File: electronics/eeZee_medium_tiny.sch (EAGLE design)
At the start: 11 parts, among them IC1 TINY24/44/84, J2 avrisp, Q1 16MHz

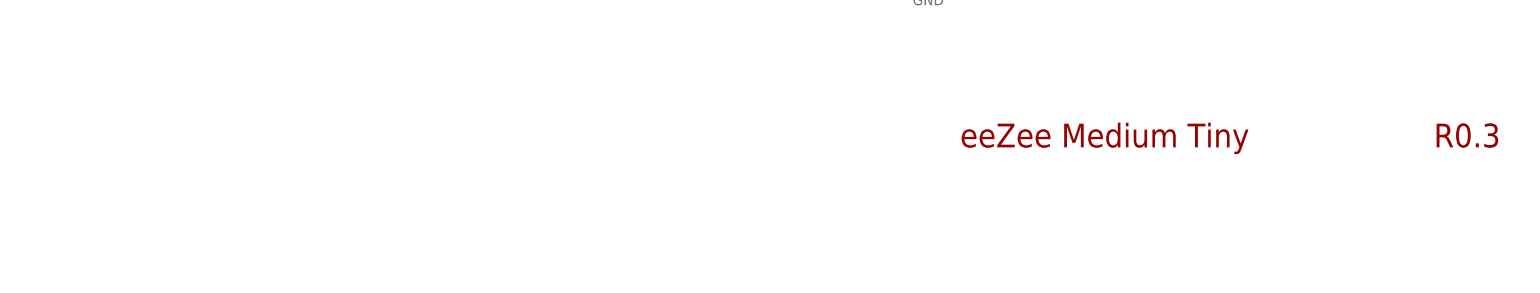
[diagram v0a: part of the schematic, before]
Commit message: update logo, silk, add help url
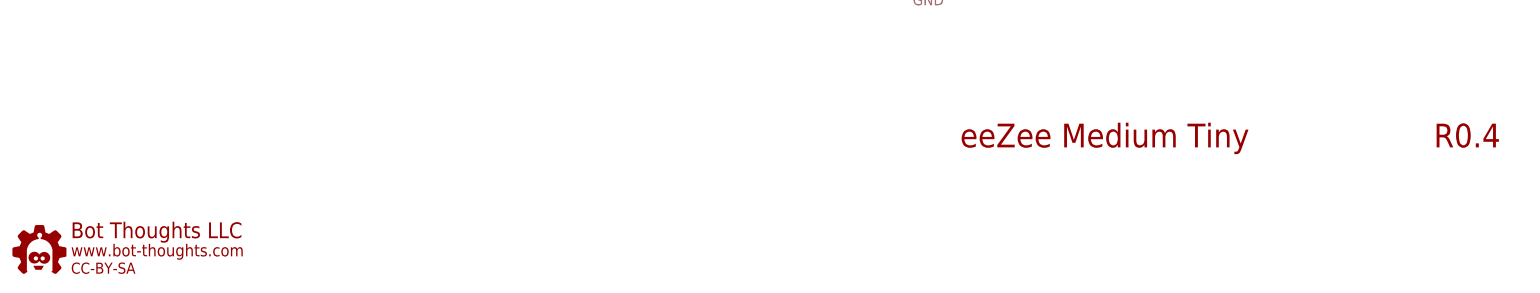
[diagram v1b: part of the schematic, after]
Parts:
- added U$1: BTLOGO-LOGO-SM, bt:BTLOGO-LOGO-SM
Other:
- note added: "R0.4"
- note removed: "R0.3"
